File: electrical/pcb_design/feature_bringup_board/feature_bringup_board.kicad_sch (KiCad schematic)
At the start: 23 parts, among them J1 Sensor Signal, J10 Molex_504050-0691, J11 Button_Socket, J12 Button_Socket, J13 Button_Socket, J2 Sensor PWR, J3 External SPI, J4 External Power, J5 Power Selection, J6 STLINK, J9 Molex_504050-0691, U1 STM32L452RCT6

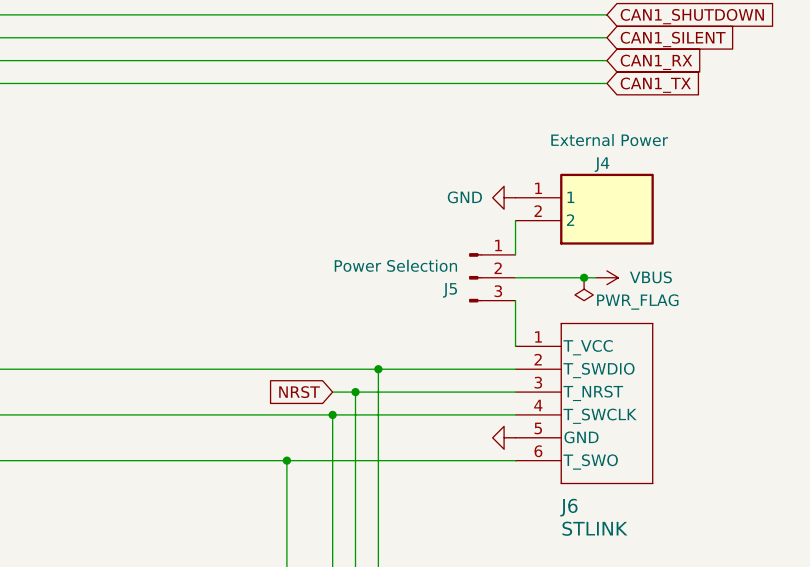
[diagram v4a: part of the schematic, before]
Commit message: Remove VBUS selection header. The ST-LINK programmer does not provide power, so we will always need external power. No selection necessary.
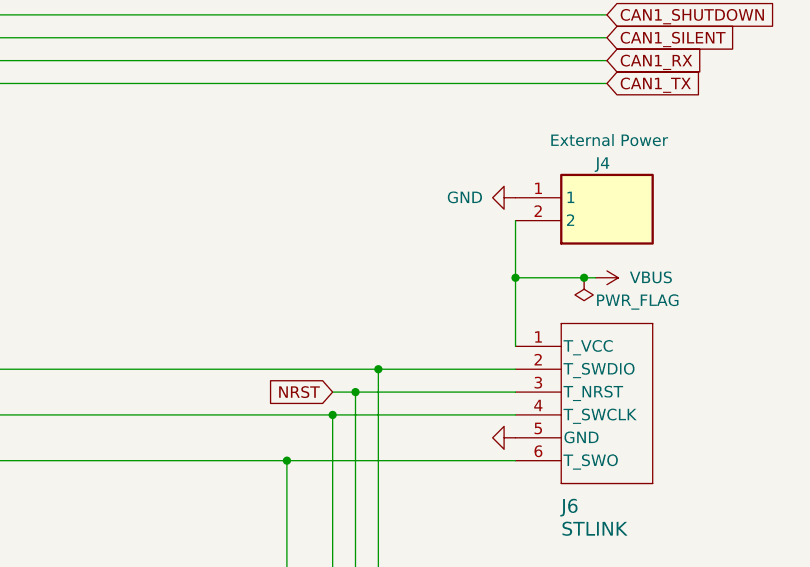
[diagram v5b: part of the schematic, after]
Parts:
- removed J5: Power Selection, Connector_PinHeader_2.54mm:PinHeader_1x03_P2.54mm_Vertical, symbol Connector:Conn_01x03_Pin
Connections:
- net VBUS: now also J4.2, J6.1 (T_VCC)
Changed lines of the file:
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@@
   (junction (at 218.44 97.79) (diameter 0) (color 0 0 0 0)
+  )
+  (junction (at 236.22 85.09) (diameter 0) (color 0 0 0 0)
   )
   (junction (at 39.37 124.46) (diameter 0) (color 0 0 0 0)
@@
     (stroke (width 0) (type default))
   )
-  (wire (pts (xy 236.22 87.63) (xy 236.22 92.71))
+  (wire (pts (xy 236.22 78.74) (xy 236.22 85.09))
     (stroke (width 0) (type default))
   )
@@
     (stroke (width 0) (type default))
   )
+  (wire (pts (xy 236.22 85.09) (xy 236.22 92.71))
+    (stroke (width 0) (type default))
+  )
   (wire (pts (xy 64.77 76.2) (xy 64.77 87.63))
-    (stroke (width 0) (type default))
-  )
-  (wire (pts (xy 236.22 78.74) (xy 236.22 82.55))
     (stroke (width 0) (type default))
   )
@@
         )
       )
-    )
-  )
-  (symbol (lib_id "Connector:Conn_01x03_Pin") (at 231.14 85.09 0) (unit 1)
-    (in_bom yes) (on_board yes) (dnp no)
-    (property "Reference" "J5" (at 229.87 86.36 0)
-      (effects (font (size 1.27 1.27)) (justify right))
-    )
-    (property "Value" "Power Selection" (at 229.87 83.82 0)
-      (effects (font (size 1.27 1.27)) (justify right))
-    )
-    (property "Footprint" "Connector_PinHeader_2.54mm:PinHeader_1x03_P2.54mm_Vertical" (at 231.14 85.09 0)
-      (effects (font (size 1.27 1.27)) hide)
-    )
-    (property "Datasheet" "~" (at 231.14 85.09 0)
-      (effects (font (size 1.27 1.27)) hide)
-    )
-    (property "MPN" "C49257" (at 231.14 85.09 0)
-      (effects (font (size 1.27 1.27)) hide)
-    )
-    (property "Active" "Y" (at 231.14 85.09 0)
-      (effects (font (size 1.27 1.27)) hide)
-    )
-    (property "Manufacturer" "BOOMELE(Boom Precision Elec)" (at 231.14 85.09 0)
-      (effects (font (size 1.27 1.27)) hide)
-    )
-    (property "Manufacturer Part Number" "2.54-1*3PPin" (at 231.14 85.09 0)
-      (effects (font (size 1.27 1.27)) hide)
-    )
-    (pin "1")
-    (pin "2")
-    (pin "3")
-    (instances
-      (project "feature_bringup_board"
-        (path "/695f882b-5312-4493-b26d-8f7d6768a9db"
-          (reference "J5") (unit 1)
-        )
-      )

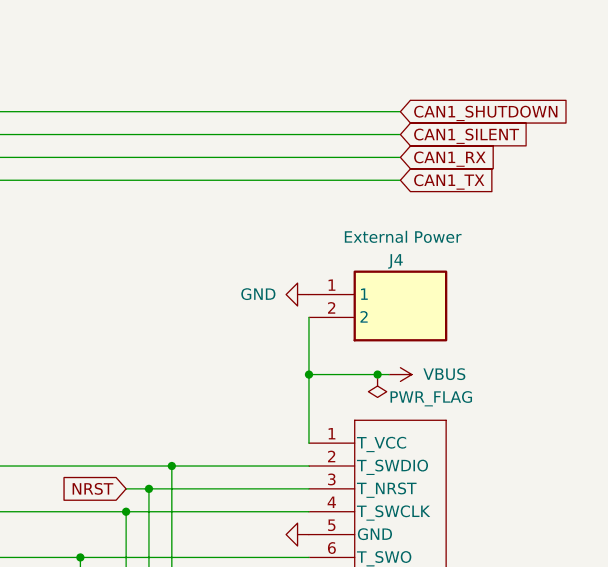
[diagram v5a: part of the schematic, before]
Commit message: Fix orientation of external power header to align with standard battery holders that also use JST PH connectors.
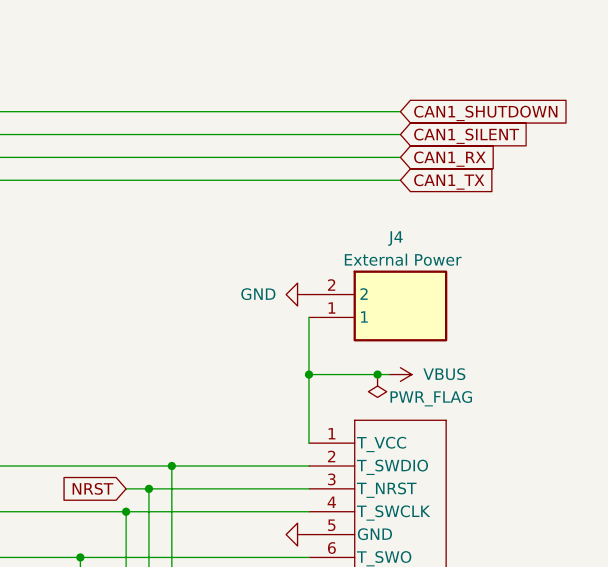
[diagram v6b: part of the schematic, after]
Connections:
- net GND: now also J4.2; no longer J4.1
- net VBUS: now also J4.1; no longer J4.2
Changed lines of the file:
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@@
+    )
+  )
+  (symbol (lib_id "TVSC:B2B-PH-K-S__LF__SN_") (at 236.22 76.2 0) (unit 1)
+    (in_bom yes) (on_board yes) (dnp no)
+    (property "Reference" "J4" (at 245.11 69.85 0)
+      (effects (font (size 1.27 1.27)) (justify left))
+    )
+    (property "Value" "External Power" (at 240.03 72.39 0)
+      (effects (font (size 1.27 1.27)) (justify left))
+    )
+    (property "Footprint" "footprints:B2BPHKSLFSN" (at 252.73 171.12 0)
+      (effects (font (size 1.27 1.27)) (justify left top) hide)
+    )
+    (property "Datasheet" "http://www.jst-mfg.com/product/pdf/eng/ePH.pdf" (at 252.73 271.12 0)
+      (effects (font (size 1.27 1.27)) (justify left top) hide)
+    )
+    (property "Height" "6" (at 252.73 471.12 0)
+      (effects (font (size 1.27 1.27)) (justify left top) hide)
+    )
+    (property "Manufacturer" "JST (JAPAN SOLDERLESS TERMINALS)" (at 252.73 571.12 0)
+      (effects (font (size 1.27 1.27)) (justify left top) hide)
+    )
+    (property "Manufacturer Part Number" "B2B-PH-K-S (LF)(SN)" (at 252.73 671.12 0)
+      (effects (font (size 1.27 1.27)) (justify left top) hide)
+    )
+    (property "Mouser Part Number" "" (at 252.73 771.12 0)
+      (effects (font (size 1.27 1.27)) (justify left top) hide)
+    )
+    (property "Mouser Price/Stock" "" (at 252.73 871.12 0)
+      (effects (font (size 1.27 1.27)) (justify left top) hide)
+    )
+    (property "Arrow Part Number" "" (at 252.73 971.12 0)
+      (effects (font (size 1.27 1.27)) (justify left top) hide)
+    )
+    (property "Arrow Price/Stock" "" (at 252.73 1071.12 0)
+      (effects (font (size 1.27 1.27)) (justify left top) hide)
+    )
+    (property "MPN" "C131337" (at 236.22 76.2 0)
+      (effects (font (size 1.27 1.27)) hide)
+    )
+    (property "Manufacturer" "JST" (at 236.22 76.2 0)
+      (effects (font (size 1.27 1.27)) hide)
+    )
+    (property "Manufacturer Part Number" "B2B-PH-K-S(LF)(SN)" (at 236.22 76.2 0)
+      (effects (font (size 1.27 1.27)) hide)
+    )
+    (property "Active" "Y" (at 236.22 76.2 0)
+      (effects (font (size 1.27 1.27)) hide)
+    )
+    (pin "1")
+    (pin "2")
+    (instances
+      (project "feature_bringup_board"
+        (path "/695f882b-5312-4493-b26d-8f7d6768a9db"
+          (reference "J4") (unit 1)
+        )
+      )
     )
   )
@@
         )
       )
-    )
-  )
-  (symbol (lib_id "TVSC:B2B-PH-K-S__LF__SN_") (at 236.22 78.74 0) (mirror x) (unit 1)
-    (in_bom yes) (on_board yes) (dnp no)
-    (property "Reference" "J4" (at 245.11 72.39 0)
-      (effects (font (size 1.27 1.27)) (justify left))
-    )
-    (property "Value" "External Power" (at 240.03 69.85 0)
-      (effects (font (size 1.27 1.27)) (justify left))
-    )
-    (property "Footprint" "footprints:B2BPHKSLFSN" (at 252.73 -16.18 0)
-      (effects (font (size 1.27 1.27)) (justify left top) hide)
-    )
-    (property "Datasheet" "http://www.jst-mfg.com/product/pdf/eng/ePH.pdf" (at 252.73 -116.18 0)
-      (effects (font (size 1.27 1.27)) (justify left top) hide)
-    )
-    (property "Height" "6" (at 252.73 -316.18 0)
-      (effects (font (size 1.27 1.27)) (justify left top) hide)
-    )
-    (property "Manufacturer" "JST (JAPAN SOLDERLESS TERMINALS)" (at 252.73 -416.18 0)
-      (effects (font (size 1.27 1.27)) (justify left top) hide)
-    )
-    (property "Manufacturer Part Number" "B2B-PH-K-S (LF)(SN)" (at 252.73 -516.18 0)
-      (effects (font (size 1.27 1.27)) (justify left top) hide)
-    )
-    (property "Mouser Part Number" "" (at 252.73 -616.18 0)
-      (effects (font (size 1.27 1.27)) (justify left top) hide)
-    )
-    (property "Mouser Price/Stock" "" (at 252.73 -716.18 0)
-      (effects (font (size 1.27 1.27)) (justify left top) hide)
-    )
-    (property "Arrow Part Number" "" (at 252.73 -816.18 0)
-      (effects (font (size 1.27 1.27)) (justify left top) hide)
-    )
-    (property "Arrow Price/Stock" "" (at 252.73 -916.18 0)
-      (effects (font (size 1.27 1.27)) (justify left top) hide)
-    )
-    (property "MPN" "C131337" (at 236.22 78.74 0)
-      (effects (font (size 1.27 1.27)) hide)
-    )
-    (property "Manufacturer" "JST" (at 236.22 78.74 0)
-      (effects (font (size 1.27 1.27)) hide)
-    )
-    (property "Manufacturer Part Number" "B2B-PH-K-S(LF)(SN)" (at 236.22 78.74 0)
-      (effects (font (size 1.27 1.27)) hide)
-    )
-    (property "Active" "Y" (at 236.22 78.74 0)
-      (effects (font (size 1.27 1.27)) hide)
-    )
-    (pin "1")
-    (pin "2")
-    (instances
-      (project "feature_bringup_board"
-        (path "/695f882b-5312-4493-b26d-8f7d6768a9db"
-          (reference "J4") (unit 1)
-        )
-      )

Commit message: Fix several small issues on feature bringup board.
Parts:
- removed J4: External Power, footprints:B2BPHKSLFSN, symbol TVSC:B2B-PH-K-S__LF__SN_
- J1, J2: Manufacturer JST -> JST (JAPAN SOLDERLESS TERMINALS); Manufacturer Part Number B2B-PH-K-S(LF)(SN) -> B2B-PH-K-S (LF)(SN)
- TP10: footprint footprints:Keystone_5001 -> footprints:Keystone_5002; MPN C238122 -> C238123; Manufacturer Part Number 5001 -> 5002
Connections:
- net VBUS is gone; now on net +3V3: J6.1 (T_VCC)

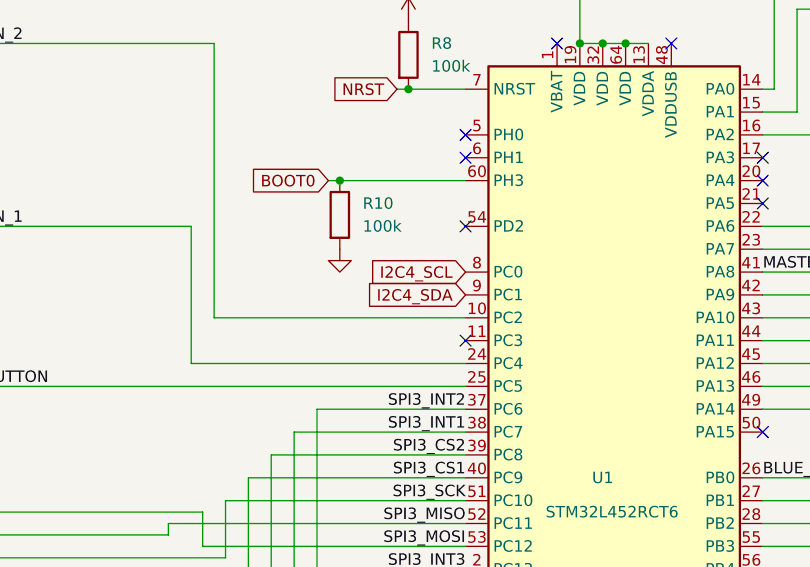
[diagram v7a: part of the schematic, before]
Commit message: Move power monitoring from I2C4 to I2C3. Note that these two buses use the same pins, and the major aspects of this change will be in software.
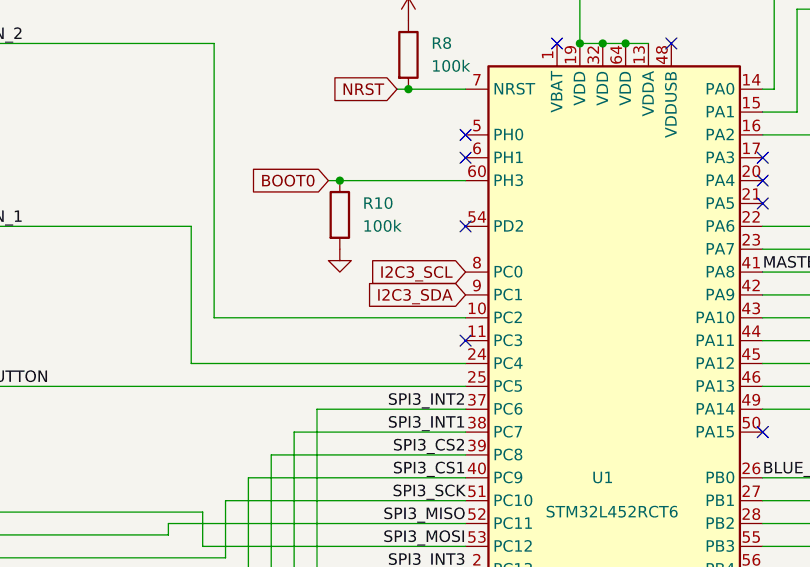
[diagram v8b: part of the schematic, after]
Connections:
- net I2C4_SCL renamed I2C3_SCL
- net I2C4_SDA renamed I2C3_SDA
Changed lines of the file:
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@@
     )
   )
-  (global_label "I2C4_SDA" (shape input) (at 88.9 55.88 180) (fields_autoplaced)
+  (global_label "I2C3_SDA" (shape input) (at 88.9 55.88 180) (fields_autoplaced)
     (effects (font (size 1.27 1.27)) (justify right))
     (property "Intersheetrefs" "${INTERSHEET_REFS}" (at 77.0853 55.88 0)
@@
     )
   )
-  (global_label "I2C4_SCL" (shape input) (at 88.9 53.34 180) (fields_autoplaced)
+  (global_label "I2C3_SCL" (shape input) (at 88.9 53.34 180) (fields_autoplaced)
     (effects (font (size 1.27 1.27)) (justify right))
     (property "Intersheetrefs" "${INTERSHEET_REFS}" (at 77.1458 53.34 0)
